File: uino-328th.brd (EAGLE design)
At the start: 68.6 x 53.3 mm, 11 parts, among them J1 USB_MICRO_B_2.0-TH

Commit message: Schematic complete.
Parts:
- removed ICSP: (no value), adilinden:2X03
- removed U$1: ATMEGA328P-UINO2-P, adi-atmega:DIL28-3
- removed U$2: PIC16F1454-P, adi-pic:DIL14
- added C10, C2, C4, C5, C6, C7, C8, C9: (no value), rc-master-th:C025-040X018
- added C3: (no value), rc-master-th:CTT-025-040
- added D2, D3, D4: (no value), SparkFun-LED:LED3MM
- added F1, F2: (no value), adi-misc:R1206
- added J2: USB_MICRO_B_2.0-TH, adi-misc:ZX62D-AB-5P8
- added J3: (no value), SparkFun-Connectors:1X06_LOCK
- added JP1, JP2: SJ-035, jumpers:SJ-035
- added JP3: (no value), adi-misc:2X03
- added R2, R3, R4, R5, R6, R7: (no value), rc-master-th:X038X018
- added T1: (no value), zetex:SOT223
- added U1: AP1117E, v-reg:SOT223
- added U2: PIC16F1454-P, adi-pic:DIL14
- added U3: ATMEGA328P-P, adi-atmega:DIL28-3
- added Y1: (no value), crystal:HC49/S
- C1: device rc-master-th:C025-040X018 -> rc-master-th:CTT-025-040
- D1: value (none) -> 1N4004-7; device led:LED3MM -> diode:DO41-7
- J1: value USB_MICRO_B_2.0-TH -> CON_TERMINAL_BLOCK_02-5MM; device adilinden:ZX62D-AB-5P8 -> dp_devices.v6:TERMINAL_BLOCK_2P_5
- R1: device rc-master-th:0204/7 -> rc-master-th:X038X018
- moved R1 150.2 mm to (11.4, 59.7)
- moved D1 116.1 mm to (21.6, 7.62), turned to 270 degrees
- moved C1 47.4 mm to (15.2, 8.89), turned to 270 degrees
- moved J1 30.6 mm to (3.81, 7.62), turned to 90 degrees
- renumbered ANALOG to JP5, IOH to JP7, IOL to JP6, POWER to JP4
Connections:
- removed net AGND: U$1.22
- removed net AVCC: U$1.20
- removed net VCC: ICSP.2, U$1.7
- removed net VDD: U$2.1
- removed net VSS: U$2.14
- removed net VUSB3V3: U$2.11
- new net CLKIN: C8.2, JP2.2, U3.9, Y1.2
- new net CLKOUT: JP2.1, U2.3
- new net DTR: JP1.1, U2.7
- new net ICSPCLK: J3.5, R4.1, U2.9
- new net ICSPDAT: J3.4, R6.1, U2.10
- new net LVP: J3.6
- new net N$10: R5.2, U2.5
- new net N$12: D2.K, R4.2
- new net N$13: D3.K, R6.2
- new net N$15: F2.2, T1.2, T1.4
- new net N$5: D4.A, R7.1
- new net N$6: J2.4
- new net N$7: C9.2, U3.10, Y1.1
- new net N$8: F1.1, J1.2
- new net N$9: R3.2, U2.6
- new net VPP: J3.1, R1.1, U2.4
- new net VUSB: F2.1, J2.1
- net 5V: now also C3.+, C4.2, C5.2, C6.2, D2.A, D3.A, J3.2, JP3.2, R1.2, R2.2, T1.3, U1.2, U1.4, U2.1, U3.20, U3.7
- net A0: now also U3.23; no longer U$1.23
- net A1: now also U3.24; no longer U$1.24
- net A2: now also U3.25; no longer U$1.25
- net A3: now also U3.26; no longer U$1.26
- net A4/SDA: now also U3.27; no longer U$1.27
- net A5/SCL: now also U3.28; no longer U$1.28
- net AREF: now also C10.2, U3.21; no longer C1.1, U$1.21
- net D0/RXD: now also R3.1, U3.2; no longer U$1.2
- net D1/TXD: now also R5.1, U3.3; no longer U$1.3
- net D10/SS: now also U3.16; no longer U$1.16
- net D11/MOSI: now also JP3.4, U3.17; no longer ICSP.4, U$1.17
- net D12/MISO: now also JP3.1, U3.18; no longer ICSP.1, U$1.18
- net D13/SCK: now also JP3.3, R7.2, U3.19; no longer ICSP.3, R1.2, U$1.19
- net D2: now also U3.4; no longer U$1.4
- net D3: now also U3.5; no longer U$1.5
- net D4: now also U3.6; no longer U$1.6
- net D5: now also U3.11; no longer U$1.11
- net D6: now also U3.12; no longer U$1.12
- net D7: now also U3.13; no longer U$1.13
- net D8: now also U3.14; no longer U$1.14
- net D9: now also U3.15; no longer U$1.15
- net GND: now also C1.-, C10.1, C2.1, C3.-, C4.1, C5.1, C6.1, C8.1, C9.1, D1.A, D4.K, J1.1, J2.5, J2.S1, J2.S2, J3.3, JP3.6, T1.1, U1.1, U2.14, U3.22, U3.8; no longer C1.2, D1.K, ICSP.6, U$1.8
- net N$1: now also C2.2, U2.11; no longer J1.2, U$2.12
- net N$2: now also C7.1, JP1.2; no longer J1.3, U$2.13
- net N$3: now also J2.2, U2.12; no longer J1.5, J1.S1
- net N$4: now also J2.3, U2.13; no longer D1.A, R1.1
- net RESET: now also C7.2, JP3.5, R2.1, U3.1; no longer ICSP.5
- net VIN: now also C1.+, D1.C, F1.2, U1.3
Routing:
- net A5/SCL: track 0.00 -> 10.7 mm
- net A4/SDA: track 0.00 -> 10.2 mm
- net A3: track 0.00 -> 10.2 mm
- net A2: track 0.00 -> 10.2 mm
- net A1: track 0.00 -> 10.2 mm
- net A0: track 0.00 -> 10.2 mm
- added copper zone on layer 1, net GND
- added copper zone on layer 16, net GND

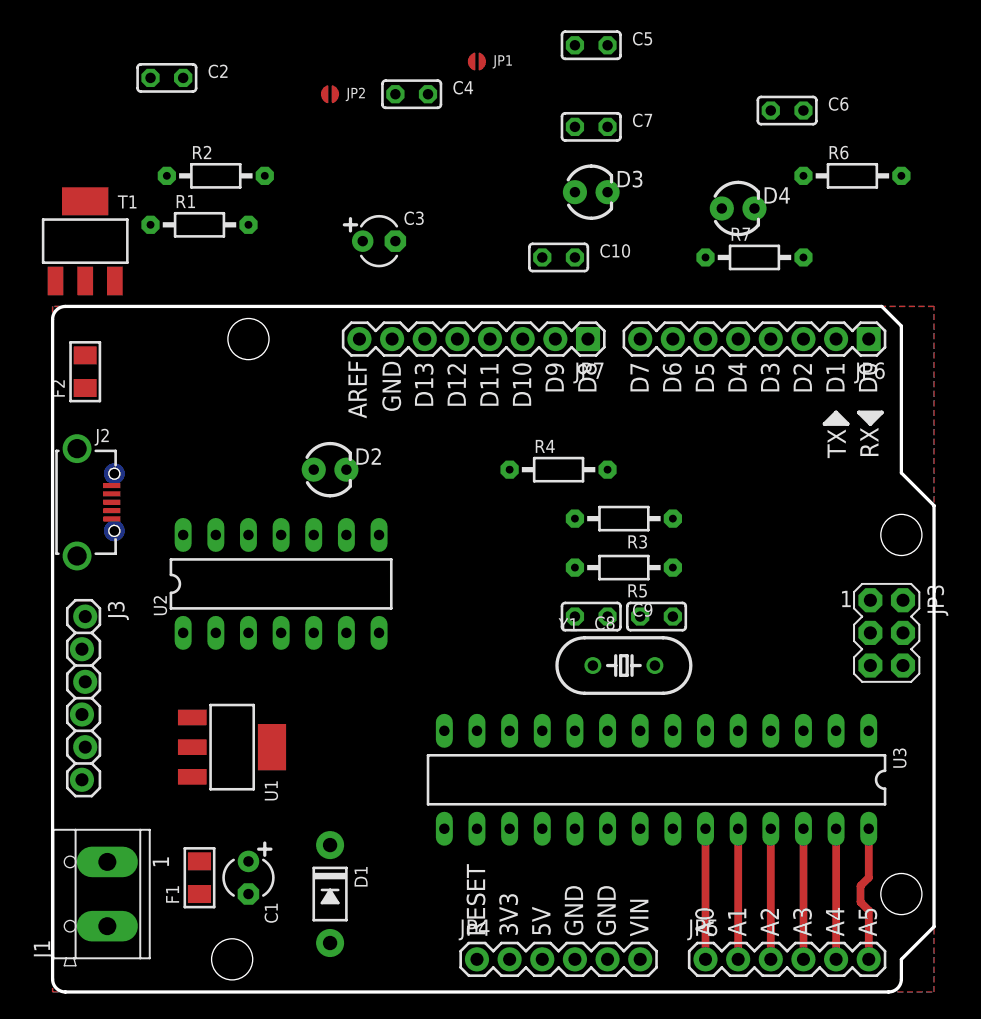
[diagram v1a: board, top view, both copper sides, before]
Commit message: Changed to 3V3 and 5V hybrid.
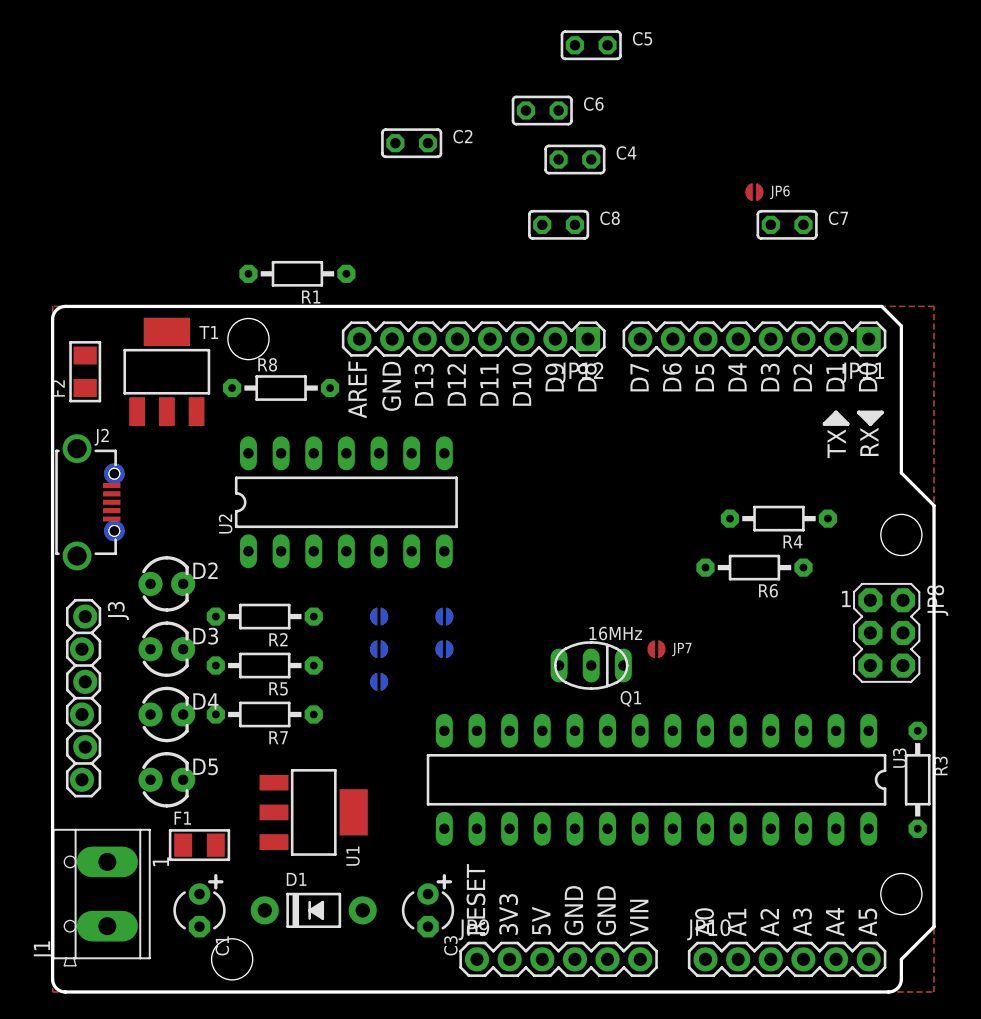
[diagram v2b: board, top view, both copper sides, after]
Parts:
- removed C10, C9: (no value), rc-master-th:C025-040X018
- removed Y1: (no value), crystal:HC49/S
- added D5: Red, SparkFun-LED:LED3MM
- added JP10, JP9: (no value), SparkFun:1X06
- added JP11, JP12: (no value), SparkFun:1X08
- added JP8: (no value), adi-misc:2X03
- added Q1: 16MHz, murata-resonators:CSTLS_X
- added R8: 1k, rc-master-th:X038X018
- C1, C3: value (none) -> 4u7
- C2, C4, C5, C6, C8: value (none) -> 100n
- D2: value (none) -> Green
- D3, D4: value (none) -> Yellow
- F1, F2: value (none) -> 500mA
- JP3: value (none) -> SJ-035; device adi-misc:2X03 -> jumpers:SJ-035
- JP4, JP5: value (none) -> SJ-035; device SparkFun:1X06 -> jumpers:SJ-035
- JP6, JP7: value (none) -> SJ-035; device SparkFun:1X08 -> jumpers:SJ-035
- R1, R3: value (none) -> 47k
- R2, R4, R5, R6, R7: value (none) -> 1k
- T1: value (none) -> NTF5P03T3G
- moved D4 59.4 mm to (8.89, 21.6)
- moved C3 52.2 mm to (29.2, 6.35), turned to 270 degrees
- moved R7 52.1 mm to (16.5, 21.6), turned to 180 degrees
- moved D3 48.5 mm to (8.89, 26.7)
- moved JP2 44.1 mm to (30.5, 26.7), flipped to the bottom
- moved JP1 43.3 mm to (30.5, 29.2), flipped to the bottom
- moved JP3 39.5 mm to (25.4, 29.2), flipped to the bottom, turned to 0 degrees
- moved JP5 35.0 mm to (25.4, 26.7), flipped to the bottom
- moved R2 34.5 mm to (16.5, 29.2), turned to 180 degrees
- moved C8 31.4 mm to (39.4, 59.7), turned to 0 degrees
- moved R6 31.4 mm to (54.6, 33.0), turned to 180 degrees
- moved R3 30.6 mm to (67.3, 16.5), turned to 270 degrees
- moved R5 29.0 mm to (16.5, 25.4)
- moved JP7 24.7 mm to (47.0, 26.7), turned to 0 degrees
- moved JP4 22.9 mm to (25.4, 24.1), flipped to the bottom
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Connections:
- new net N$11: Q1.3, U3.10
- new net VCC: C3.+, C4.2, C5.2, C6.2, D2.A, D3.A, D4.A, J3.2, JP1.2, JP2.1, JP4.1, JP5.1, JP8.2, R1.2, R3.2, U1.2, U1.4, U2.1, U3.20, U3.7
- new net VPIC: C2.2, JP5.2, U2.11
- net 3V3: now also JP9.2
- net 5V: now also JP2.2, JP9.3; no longer C3.+, C4.2, C5.2, C6.2, D2.A, D3.A, J3.2, JP3.2, JP4.3, R1.2, R2.2, T1.3, U1.2, U1.4, U2.1, U3.20, U3.7
- net A0: now also JP10.1; no longer JP5.1
- net A1: now also JP10.2; no longer JP5.2
- net A2: now also JP10.3; no longer JP5.3
- net A3: now also JP10.4; no longer JP5.4
- net A4/SDA: now also JP10.5; no longer JP5.5
- net A5/SCL: now also JP10.6; no longer JP5.6
- net AREF: now also C8.2, JP12.8; no longer C10.2, JP7.8
- net CLKIN: now also JP7.2, Q1.1; no longer C8.2, JP2.2, Y1.2
- net CLKOUT: now also JP7.1; no longer JP2.1
- net D0/RXD: now also JP11.1, R4.1; no longer JP6.1, R3.1
- net D1/TXD: now also JP11.2, R6.1; no longer JP6.2, R5.1
- net D10/SS: now also JP12.3; no longer JP7.3
- net D11/MOSI: now also JP12.4, JP8.4; no longer JP3.4, JP7.4
- net D12/MISO: now also JP12.5, JP8.1; no longer JP3.1, JP7.5
- net D13/SCK: now also JP12.6, JP8.3, R8.2; no longer JP3.3, JP7.6, R7.2
- net D2: now also JP11.3; no longer JP6.3
- net D3: now also JP11.4; no longer JP6.4
- net D4: now also JP11.5; no longer JP6.5
- net D5: now also JP11.6; no longer JP6.6
- net D6: now also JP11.7; no longer JP6.7
- net D7: now also JP11.8; no longer JP6.8
- net D8: now also JP12.1; no longer JP7.1
- net D9: now also JP12.2; no longer JP7.2
- net DTR: now also JP6.1; no longer JP1.1
- net GND: now also D5.K, JP12.7, JP8.6, JP9.4, JP9.5, Q1.2, R2.1; no longer C10.1, C9.1, D4.K, JP3.6, JP4.4, JP4.5, JP7.7
- net ICSPCLK: now also R5.1; no longer R4.1
- net ICSPDAT: now also R7.1; no longer R6.1
- net N$1: now also D2.K, R2.2; no longer C2.2, U2.11
- net N$10: now also R6.2; no longer R5.2
- net N$12: now also D3.K, R5.2; no longer D2.K, R4.2
- net N$13: now also D4.K, R7.2; no longer D3.K, R6.2
- net N$2: now also JP6.2; no longer JP1.2
- net N$5: now also D5.A, R8.1; no longer D4.A, R7.1
- net N$7: now also F2.1, J2.1; no longer C9.2, U3.10, Y1.1
- net N$9: now also R4.2; no longer R3.2
- net RESET: now also JP8.5, JP9.1, R3.1; no longer JP3.5, JP4.1, R2.1
- net VIN: now also JP3.2, JP9.6; no longer JP4.6
- net VUSB: now also JP1.1, JP3.1, T1.3; no longer F2.1, J2.1
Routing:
- net A5/SCL: track 10.7 -> 0.00 mm
- net A4/SDA: track 10.2 -> 0.00 mm
- net A3: track 10.2 -> 0.00 mm
- net A2: track 10.2 -> 0.00 mm
- net A1: track 10.2 -> 0.00 mm
- net A0: track 10.2 -> 0.00 mm

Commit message: Attempts at routing board.
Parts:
- R1, R2, R3, R5, R7: device rc-master-th:X038X018 -> rc-master:0207/7
- R4, R6, R8: device rc-master-th:X038X018 -> rc-master:0207/10
- moved C8 50.1 mm to (47.0, 10.2), turned to 180 degrees
- moved C5 45.9 mm to (11.4, 39.4), turned to 270 degrees
- moved C4 41.6 mm to (49.5, 24.1), turned to 270 degrees
- moved JP6 31.4 mm to (38.1, 35.6), flipped to the bottom, turned to 180 degrees
- moved R8 28.2 mm to (34.3, 24.1)
- moved C7 27.6 mm to (43.8, 35.6)
- moved R1 24.3 mm to (16.5, 31.8)
- moved C6 22.9 mm to (19.1, 55.9)
- moved C2 20.5 mm to (20.3, 47.0), turned to 270 degrees
- moved Q1 2.84 mm to (44.5, 24.1)
- moved D1 2.84 mm to (21.6, 3.81)
- moved JP7 1.80 mm to (45.7, 27.9), flipped to the bottom, turned to 180 degrees
- moved U2 1.80 mm to (21.6, 39.4)
- moved U1 1.27 mm to (20.3, 12.7)
- moved JP1 1.27 mm to (30.5, 30.5)
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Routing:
- net D13/SCK: track 0.00 -> 43.3 mm, vias 0 -> 1
- net D9: track 0.00 -> 42.7 mm
- net D12/MISO: track 0.00 -> 42.6 mm, vias 0 -> 2
- net D11/MOSI: track 0.00 -> 41.6 mm, vias 0 -> 2
- net D10/SS: track 0.00 -> 41.2 mm, vias 0 -> 2
- net D7: track 0.00 -> 35.7 mm
- net D8: track 0.00 -> 35.1 mm
- net CLKOUT: track 0.00 -> 34.0 mm
- net D6: track 0.00 -> 32.8 mm
- net D5: track 0.00 -> 32.8 mm
- net D4: track 0.00 -> 31.5 mm
- net D2: track 0.00 -> 31.5 mm
- net D1/TXD: track 0.00 -> 31.5 mm
- net D0/RXD: track 0.00 -> 31.5 mm
- net D3: track 0.00 -> 30.3 mm
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
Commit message: First cut to try gerber.
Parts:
- removed C6: 100n, rc-master-th:C025-040X018
- removed JP10, JP9: (no value), SparkFun:1X06
- removed JP11, JP12: (no value), SparkFun:1X08
- removed JP8: (no value), adi-misc:2X03
- removed T1: NTF5P03T3G, zetex:SOT223
- added D6: Red, SparkFun-LED:LED3MM
- added S1: TL1100X, adi-misc:TL1100X
- D1: value 1N4004-7 -> (none); device diode:DO41-7 -> diode:DO35-7
- D2: value Green -> (none); device SparkFun-LED:LED3MM -> diode:DO35-7
- D3: value Yellow -> Green
- D5: value Red -> Yellow
- F1, F2: device adi-misc:R1206 -> adi-misc:PTC
- J1: device dp_devices.v6:TERMINAL_BLOCK_2P_5 -> adi-misc:TERMINAL_BLOCK_2P_5
- JP3: value SJ-035 -> (none); device jumpers:SJ-035 -> adi-misc:2X03
- JP4, JP5: value SJ-035 -> (none); device jumpers:SJ-035 -> SparkFun:1X06
- JP6, JP7: value SJ-035 -> (none); device jumpers:SJ-035 -> SparkFun:1X08
- Q1: value 16MHz -> (none)
- U1: value AP1117E -> V_REG_MCP170X; device v-reg:SOT223 -> adi-misc:TO-92
- moved C5 42.4 mm to (41.9, 9.84), turned to 0 degrees
- moved F2 39.8 mm to (14.0, 10.2)
- moved JP3 39.6 mm to (64.9, 27.9), flipped to the top, turned to 270 degrees
- moved JP5 35.9 mm to (50.8, 2.54), flipped to the top
- moved JP6 29.6 mm to (63.5, 50.8), flipped to the top
- moved D2 27.9 mm to (22.9, 7.62)
- moved JP4 24.1 mm to (33.0, 2.54), flipped to the top
- moved JP7 23.2 mm to (41.7, 50.8), flipped to the top
- moved F1 21.6 mm to (25.4, 27.9), turned to 270 degrees
- moved JP2 14.2 mm to (43.2, 34.3), turned to 180 degrees
- moved C3 13.7 mm to (24.1, 19.1), turned to 90 degrees
- moved R3 12.7 mm to (55.9, 9.84), turned to 180 degrees
- moved C2 12.6 mm to (11.4, 38.1)
- moved JP1 12.3 mm to (40.6, 37.5), turned to 180 degrees
- moved D5 10.2 mm to (8.89, 26.7)
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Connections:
- removed net 3V3: JP4.2, JP9.2
- removed net N$15: F2.2, T1.2, T1.4
- removed net N$7: F2.1, J2.1
- removed net VPIC: C2.2, JP5.2, U2.11
- removed net VUSB: JP1.1, JP3.1, T1.3
- new net N$14: D2.A, F1.P$2
- new net VBUS: F1.P$1, J2.1
- net 5V: now also JP4.3; no longer JP2.2, JP9.3
- net A0: now also JP5.1; no longer JP10.1
- net A1: now also JP5.2; no longer JP10.2
- net A2: now also JP5.3; no longer JP10.3
- net A3: now also JP5.4; no longer JP10.4
- net A4/SDA: now also JP5.5; no longer JP10.5
- net A5/SCL: now also JP5.6; no longer JP10.6
- net AREF: now also JP7.8; no longer JP12.8
- net CLKIN: now also JP2.2; no longer JP7.2
- net CLKOUT: now also JP2.1; no longer JP7.1
- net D0/RXD: now also JP6.1; no longer JP11.1
- net D1/TXD: now also JP6.2; no longer JP11.2
- net D10/SS: now also JP7.3; no longer JP12.3
- net D11/MOSI: now also JP3.4, JP7.4; no longer JP12.4, JP8.4
- net D12/MISO: now also JP3.1, JP7.5; no longer JP12.5, JP8.1
- net D13/SCK: now also JP3.3, JP7.6; no longer JP12.6, JP8.3
- net D2: now also JP6.3; no longer JP11.3
- net D3: now also JP6.4; no longer JP11.4
- net D4: now also JP6.5; no longer JP11.5
- net D5: now also JP6.6; no longer JP11.6
- net D6: now also JP6.7; no longer JP11.7
- net D7: now also JP6.8; no longer JP11.8
- net D8: now also JP7.1; no longer JP12.1
- net D9: now also JP7.2; no longer JP12.2
- net DTR: now also JP1.1; no longer JP6.1
- net GND: now also D6.K, JP3.6, JP4.4, JP4.5, JP7.7, S1.1, S1.2; no longer C6.1, D5.K, JP12.7, JP8.6, JP9.4, JP9.5, T1.1
- net N$1: now also D3.K; no longer D2.K
- net N$12: now also D4.K; no longer D3.K
- net N$13: now also D5.K; no longer D4.K
- net N$2: now also JP1.2; no longer JP6.2
- net N$5: now also D6.A; no longer D5.A
- net N$8: now also F2.P$1; no longer F1.1
- net RESET: now also JP3.5, JP4.1, S1.3, S1.4; no longer JP8.5, JP9.1
- net VCC: now also C2.2, D5.A, JP3.2, JP4.2, U1.3, U2.11; no longer C6.2, D2.A, JP1.2, JP2.1, JP4.1, JP5.1, JP8.2, U1.2, U1.4
- net VIN: now also D2.C, F2.P$2, JP4.6, U1.2; no longer F1.2, JP3.2, JP9.6, U1.3
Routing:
- net VCC: track 0.00 -> 195.0 mm
- net RESET: track 0.00 -> 138.2 mm, vias 0 -> 1
- net AREF: track 0.00 -> 71.9 mm
- net D11/MOSI: track 41.6 -> 97.8 mm, vias 2 -> 1
- net D13/SCK: track 43.3 -> 95.7 mm
- net ICSPCLK: track 0.00 -> 50.5 mm
- net VIN: track 0.00 -> 50.0 mm
- net D12/MISO: track 42.6 -> 92.6 mm, vias 2 -> 1
- net ICSPDAT: track 0.00 -> 42.6 mm
- net VBUS: track 0.00 -> 30.7 mm, vias 0 -> 1
- net N$5: track 0.00 -> 28.4 mm
- net D9: track 42.7 -> 66.0 mm
- net VPP: track 0.00 -> 23.2 mm, vias 0 -> 1
- net D8: track 35.1 -> 56.5 mm
- net N$14: track 0.00 -> 18.3 mm
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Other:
- board text added: "*uino-328th"
- board text added: "by Adi Linden"
- board text added: "v0.3 2016/10/30"
